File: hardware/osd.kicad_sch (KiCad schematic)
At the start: 12 parts, among them U14 SN74LVC1G3157, U15 TLV7031

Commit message: Trim BOM to strictly needed parts, fill sourcing fields, fix library datasheets
Owner review 2026-10-11, schematic only (board not resynced).

Removed (17 parts): D1 TVS (clamps above every IC abs max), R2/R3/C5
INA186 input RC, U5 TPS22810 O4 switch with C16/C129/R9/R10/R87/D2
(VHD pad now on +5V_BST, as Matrix HD boards; HD_EN still holds the
analog VTX off via Q28, R11 kept), R67 selector (PA_VCC is +BATT),
TH1/R70 PA NTC and R84 (patched-ELRS only; GPIO37/GPIO4 no-connect),
C92 and C121 (beyond SX1281 / LP5912 datasheet decoupling).

Changed: D4 WS2812 VDD to +5V (3.5 V min); X3 TCXO pin 1 floating per
the YXC sheet; C122/C123/C134 4.7 uF 0402 -> 0201 GRM035R60J475ME15D.

Sourcing: LCSC numbers for 21 MPN lines (SKUBAAE010 has no listing);
every BOM part keeps MPN + Manufacturer for NextPCB.

Library: 16 unused lib symbols pruned; dead or HTML-only datasheet
links replaced with verified PDF URLs (RTC6705, SE5004L, FL2, X1,
EFM8BB51, BC857BM, FTC252012, HCS1206 shunt, Molex 53047).

Net-class patterns and contract entries for the removed nets dropped;
PINMAP ESP32 rows updated (GPIO36 is ADC1_CH0).

Validation: ERC 0 errors / 2 warnings (baseline); check_netlist 7 ok;
sch_integrate --check idempotent; check_conventions unchanged.

Co-Authored-By: Claude Opus 5.5 <noreply@anthropic.com>
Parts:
- C66: LCSC (none) -> C76922
- R52: LCSC (none) -> C155736
- R54: LCSC (none) -> C295793
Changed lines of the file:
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@@
 		(in_pos_files no)
 		(dnp no)
-		(property "Reference" "#PWR147"
+		(property "Reference" "#PWR138"
 			(at 158.75 69.85 0)
 			(hide yes)
@@
 			(project "OpenAIO-Whoop"
 				(path "/2c3a7206-1e66-4d43-a02f-491225e20dd6/d622c956-8c4e-5ac1-b8c4-8a8024f124d6"
-					(reference "#PWR147")
+					(reference "#PWR138")
 					(unit 1)
 				)
@@
 		(in_pos_files no)
 		(dnp no)
-		(property "Reference" "#PWR148"
+		(property "Reference" "#PWR139"
 			(at 54.61 72.39 0)
 			(hide yes)
@@
 			(project "OpenAIO-Whoop"
 				(path "/2c3a7206-1e66-4d43-a02f-491225e20dd6/d622c956-8c4e-5ac1-b8c4-8a8024f124d6"
-					(reference "#PWR148")
+					(reference "#PWR139")
 					(unit 1)
 				)
@@
 		(in_pos_files no)
 		(dnp no)
-		(property "Reference" "#PWR157"
+		(property "Reference" "#PWR148"
 			(at 106.68 119.38 0)
 			(hide yes)
@@
 			(project "OpenAIO-Whoop"
 				(path "/2c3a7206-1e66-4d43-a02f-491225e20dd6/d622c956-8c4e-5ac1-b8c4-8a8024f124d6"
-					(reference "#PWR157")
+					(reference "#PWR148")
 					(unit 1)
 				)
@@
 		(in_pos_files no)
 		(dnp no)
-		(property "Reference" "#PWR149"
+		(property "Reference" "#PWR140"
 			(at 63.5 72.39 0)
 			(hide yes)
@@
 			(project "OpenAIO-Whoop"
 				(path "/2c3a7206-1e66-4d43-a02f-491225e20dd6/d622c956-8c4e-5ac1-b8c4-8a8024f124d6"
-					(reference "#PWR149")
+					(reference "#PWR140")
 					(unit 1)
 				)
@@
 		(in_pos_files no)
 		(dnp no)
-		(property "Reference" "#PWR158"
+		(property "Reference" "#PWR149"
 			(at 66.04 135.89 0)
 			(hide yes)
@@
 			(project "OpenAIO-Whoop"
 				(path "/2c3a7206-1e66-4d43-a02f-491225e20dd6/d622c956-8c4e-5ac1-b8c4-8a8024f124d6"
-					(reference "#PWR158")
+					(reference "#PWR149")
 					(unit 1)
 				)
@@
 		(in_pos_files no)
 		(dnp no)
-		(property "Reference" "#PWR146"
+		(property "Reference" "#PWR137"
 			(at 184.15 59.69 0)
 			(hide yes)
@@
 			(project "OpenAIO-Whoop"
 				(path "/2c3a7206-1e66-4d43-a02f-491225e20dd6/d622c956-8c4e-5ac1-b8c4-8a8024f124d6"
-					(reference "#PWR146")
+					(reference "#PWR137")
 					(unit 1)
 				)
@@
 			)
 		)
-		(property "LCSC" ""
+		(property "LCSC" "C155736"
 			(at 54.61 119.38 0)
 			(hide yes)
@@
 		(in_pos_files no)
 		(dnp no)
-		(property "Reference" "#PWR154"
+		(property "Reference" "#PWR145"
 			(at 106.68 93.98 0)
 			(hide yes)
@@
 			(project "OpenAIO-Whoop"
 				(path "/2c3a7206-1e66-4d43-a02f-491225e20dd6/d622c956-8c4e-5ac1-b8c4-8a8024f124d6"
-					(reference "#PWR154")
+					(reference "#PWR145")
 					(unit 1)
 				)
@@
 		(in_pos_files no)
 		(dnp no)
-		(property "Reference" "#PWR156"
+		(property "Reference" "#PWR147"
 			(at 66.04 113.03 0)
 			(hide yes)
@@
 			(project "OpenAIO-Whoop"
 				(path "/2c3a7206-1e66-4d43-a02f-491225e20dd6/d622c956-8c4e-5ac1-b8c4-8a8024f124d6"
-					(reference "#PWR156")
+					(reference "#PWR147")
 					(unit 1)
 				)
@@
 			)
 		)
-		(property "LCSC" ""
+		(property "LCSC" "C295793"
 			(at 66.04 125.73 0)
 			(hide yes)
@@
 			)
 		)
-		(property "LCSC" ""
+		(property "LCSC" "C76922"
 			(at 63.5 62.23 0)
 			(hide yes)
@@
 		(in_pos_files no)
 		(dnp no)
-		(property "Reference" "#PWR151"
+		(property "Reference" "#PWR142"
 			(at 125.73 72.39 0)
 			(hide yes)
@@
 			(project "OpenAIO-Whoop"
 				(path "/2c3a7206-1e66-4d43-a02f-491225e20dd6/d622c956-8c4e-5ac1-b8c4-8a8024f124d6"
-					(reference "#PWR151")
+					(reference "#PWR142")
 					(unit 1)
 				)
@@
 		(in_pos_files no)
 		(dnp no)
-		(property "Reference" "#PWR155"
+		(property "Reference" "#PWR146"
 			(at 91.44 100.33 0)
 			(hide yes)
@@
 			(project "OpenAIO-Whoop"
 				(path "/2c3a7206-1e66-4d43-a02f-491225e20dd6/d622c956-8c4e-5ac1-b8c4-8a8024f124d6"
-					(reference "#PWR155")
+					(reference "#PWR146")
 					(unit 1)
 				)
@@
 		(in_pos_files no)
 		(dnp no)
-		(property "Reference" "#PWR153"
+		(property "Reference" "#PWR144"
 			(at 91.44 90.17 0)
 			(hide yes)
@@
 			(project "OpenAIO-Whoop"
 				(path "/2c3a7206-1e66-4d43-a02f-491225e20dd6/d622c956-8c4e-5ac1-b8c4-8a8024f124d6"
-					(reference "#PWR153")
+					(reference "#PWR144")
 					(unit 1)
 				)
@@
 		(in_pos_files no)
 		(dnp no)
-		(property "Reference" "#PWR150"
+		(property "Reference" "#PWR141"
 			(at 93.98 72.39 0)
 			(hide yes)
@@
 			(project "OpenAIO-Whoop"
 				(path "/2c3a7206-1e66-4d43-a02f-491225e20dd6/d622c956-8c4e-5ac1-b8c4-8a8024f124d6"
-					(reference "#PWR150")
+					(reference "#PWR141")
 					(unit 1)
 				)
@@
 		(in_pos_files no)
 		(dnp no)
-		(property "Reference" "#PWR152"
+		(property "Reference" "#PWR143"
 			(at 176.53 72.39 0)
 			(hide yes)
@@
 			(project "OpenAIO-Whoop"
 				(path "/2c3a7206-1e66-4d43-a02f-491225e20dd6/d622c956-8c4e-5ac1-b8c4-8a8024f124d6"
-					(reference "#PWR152")
-					(unit 1)
-				)
+					(reference "#PWR143")
+					(unit 1)
+				)

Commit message: Footprint audit vs datasheets, 0201 lands to Murata minimum, schematic notes shortened
Footprints: 45 checked against their datasheets by group, no pin or
land errors. C/R/L_0201_..._L pad height 0.28 -> 0.30 (Murata GRM03
reflow table c >= 0.30); other lands already at least density per D109
and left unchanged. Land spec texts cleaned (sources, shared parts).

Schematic notes: 157 -> 152 items, 19.5k -> 9.7k characters, all
current (diode-OR, removed parts, RTC6705 filters, TX0/RX0).

check_footprint 107/107 lib specs PASS; ERC 0 errors / 2 warnings;
check_netlist 7 ok; sch_integrate --check clean. Board not synced.

Co-Authored-By: Claude Opus 5.5 <noreply@anthropic.com>
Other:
- note added: "Comparator: OSD_SYNC low during sync (GPIO23, PIO2)"
- note added: "OSD_W selects white (high) or black (low) through the divider"
- note added: "Sync detection: sync tips clamped to -VF"
- note added: "U15 V+ (2) is decoupled by C70, shared with U14"
- note removed: "Comparator: OSD_SYNC low during sync, read by RP2354A PIO2 (GPIO23)"
- note removed: "Resistor divider lets the OSD_W GPIO select white (high: 1.05 V) or black (low: 0.27 V)"
- note removed: "Sync detection, VID_DC sync tips clamped to -VF (about -0.1..-0.2 V)"
- note removed: "U15 V+ (2) is decoupled by C70 in the switch cell, one 100n shared with U14 (BR-13)"
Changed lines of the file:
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@@
 		)
 	)
-	(text "Resistor divider lets the OSD_W GPIO select\nwhite (high: 1.05 V) or black (low: 0.27 V)"
+	(text "OSD_W selects white (high) or black (low) through the divider"
 		(exclude_from_sim no)
 		(at 44.958 88.392 0)
@@
 		)
 	)
-	(text "U15 V+ (2) is decoupled by C70 in the switch cell,\none 100n shared with U14 (BR-13)"
+	(text "U15 V+ (2) is decoupled by C70, shared with U14"
 		(exclude_from_sim no)
 		(at 163.83 35.56 0)
@@
 		)
 	)
-	(text "Sync detection, VID_DC sync tips\nclamped to -VF (about -0.1..-0.2 V)"
+	(text "Sync detection: sync tips clamped to -VF"
 		(exclude_from_sim no)
 		(at 157.988 20.828 0)
@@
 		)
 	)
-	(text "Comparator: OSD_SYNC low during sync,\nread by RP2354A PIO2 (GPIO23)"
+	(text "Comparator: OSD_SYNC low during sync (GPIO23, PIO2)"
 		(exclude_from_sim no)
 		(at 164.338 74.676 0)
@@
 		)
 	)
-	(text_box "Placement: C70 is the one supply cap of U14 and U15, place it between them. Video entry parts R51/C66 at the CAM pad line; video on L1/L6 over GND, never L3; away from the boost (D69). Analog class on the video nets; OSD_W / OSD_EN Default."
+	(text_box "C70 is the one supply cap of U14 and U15: place it between them. R51/C66 at the CAM pad line; video on L1/L6 over GND, away from the boost."
 		(exclude_from_sim no)
 		(at 15.24 149.86 0)
@@
 		)
 	)
-	(text_box "Copied from OpenFC-Lite-Mini osd (flown): 75R termination, 680R/470p chroma filter, sync-tip clamp, TLV7031 sync comparator, SN74LVC1G3157 camera/OSD switch. Changed: COS8051 buffer deleted, divider R52-R54 about 5x lower (P4-10), one shared C70 (D52).\nOperation: OSD_EN low (reset) -> camera passes through; OSD_EN high -> OSD_W high = white, low = black. No OSD without camera sync. OSD_W/EN/SYNC = GPIO21/22/23 (PIO2).\nC68 X5R carries <= 0.6 V DC, no DC-bias loss (D69)."
+	(text_box "OSD_EN low (reset): camera passes through. OSD_EN high: OSD_W high = white, low = black. No OSD without camera sync.\nOSD_W/EN/SYNC = GPIO21/22/23 (PIO2)."
 		(exclude_from_sim no)
 		(at 200.66 17.78 0)
@@
 		)
 	)
-	(text_box "VIDEO_OUT drives the VTX video network directly (house buffer deleted). Loaded OSD levels: black about 0.24 V, white about 0.92 V; OSD text slightly softer than the camera, accepted. V9 checks on a monitor; fallback: rescale R52-R54 within the 3 mA OSD_W budget."
+	(text_box "VIDEO_OUT drives the VTX video network directly. Loaded levels: black about 0.24 V, white about 0.92 V."
 		(exclude_from_sim no)
 		(at 133.35 86.36 0)

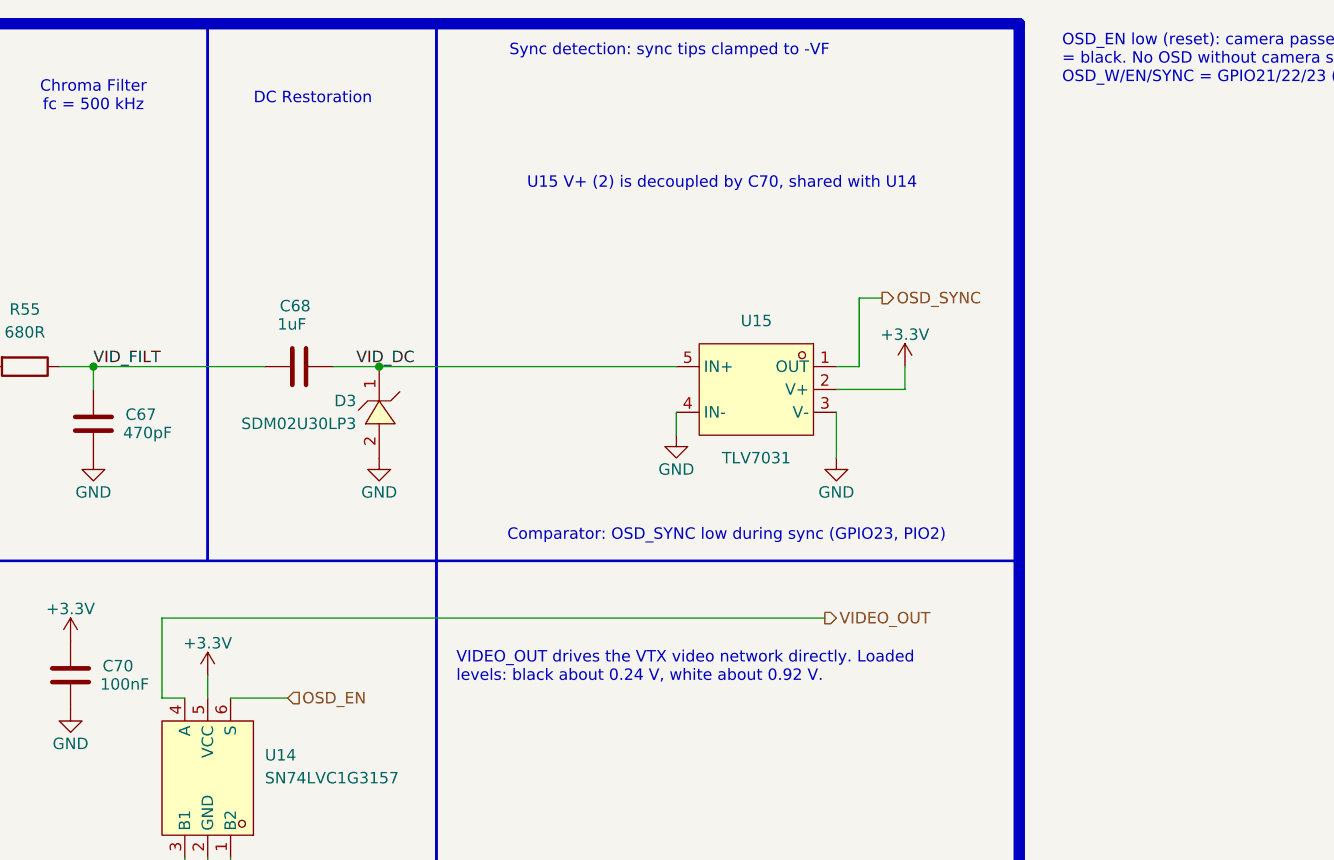
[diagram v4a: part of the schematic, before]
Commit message: WIP placement and schematic snapshot for shared routing
Owner placement and schematic edits, firmware bindings, routing notes and
board tooling, so others can try the routing. Not DRC-clean; PCB not yet
updated from the schematic (R1 to R2, C1/C2/C134 removal).

Co-Authored-By: Claude Opus 5.5 <noreply@anthropic.com>
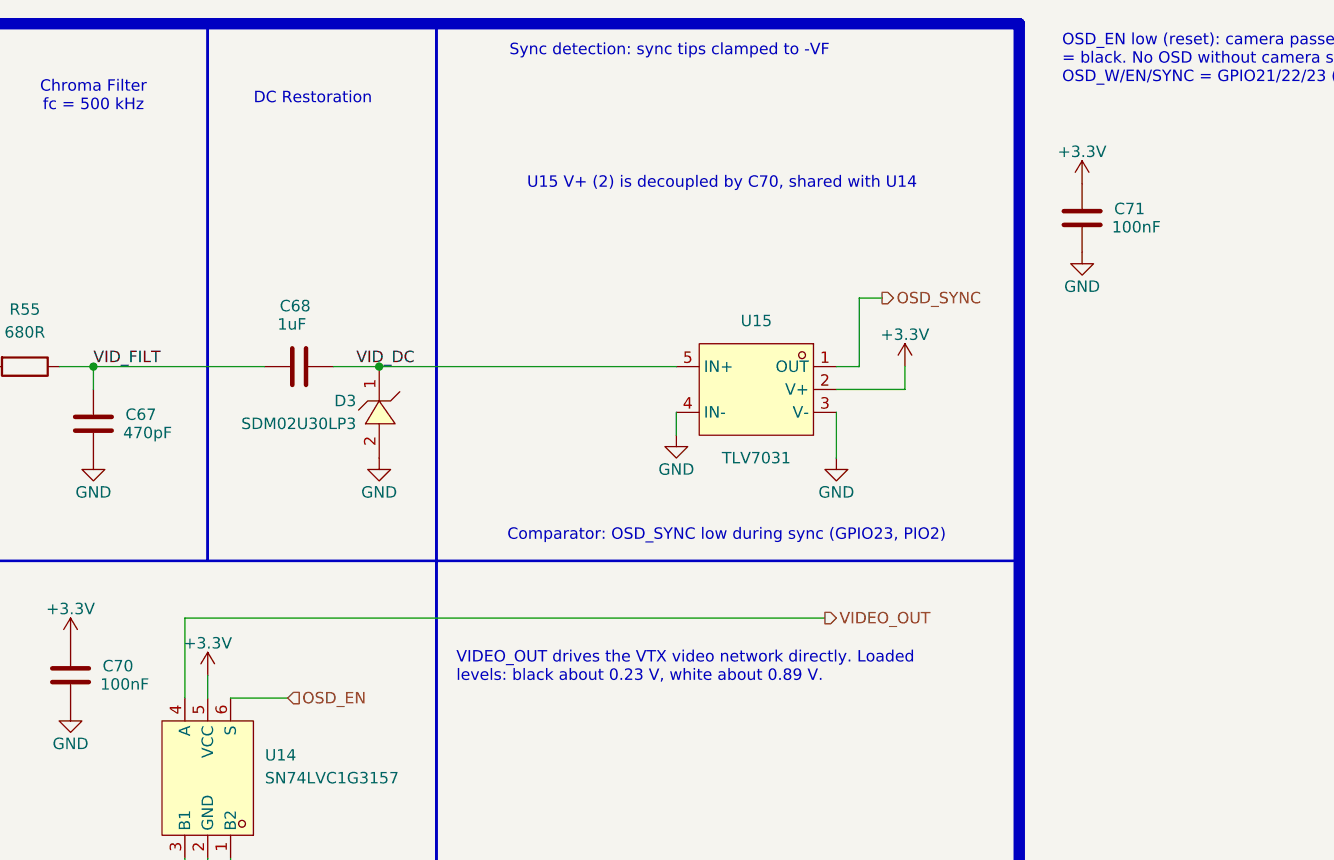
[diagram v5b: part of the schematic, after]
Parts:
- added C71: 100nF, lib:C_0201_0603Metric_L, symbol Device:C
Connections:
- net +3.3V: now also C71.1
- net GND: now also C71.2

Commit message: Every schematic symbol project-local (Device, power, Connector, Mechanical moved into lib)
tools/localise_symbols.py from OpenAIO. Netlist identical, ERC unchanged (0 errors, 24 warnings), every symbol, footprint and 3D model resolves inside the repo.

Co-Authored-By: Claude Opus 5.5 <noreply@anthropic.com>
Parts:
- C66, C67, C68, C70, C71: symbol Device:C -> lib:C
- R51, R52, R53, R54, R55: symbol Device:R -> lib:R
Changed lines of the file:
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@@
 	)
 	(symbol
-		(lib_id "power:GND")
+		(lib_id "lib:GND")
 		(at 158.75 63.5 0)
 		(unit 1)
@@
 	)
 	(symbol
-		(lib_id "power:GND")
+		(lib_id "lib:GND")
 		(at 54.61 66.04 0)
 		(unit 1)
@@
 	)
 	(symbol
-		(lib_id "Device:C")
+		(lib_id "lib:C")
 		(at 203.835 39.37 0)
 		(unit 1)
@@
 	)
 	(symbol
-		(lib_id "power:GND")
+		(lib_id "lib:GND")
 		(at 106.68 113.03 0)
 		(unit 1)
@@
 	)
 	(symbol
-		(lib_id "power:GND")
+		(lib_id "lib:GND")
 		(at 63.5 66.04 0)
 		(unit 1)
@@
 	)
 	(symbol
-		(lib_id "Device:R")
+		(lib_id "lib:R")
 		(at 54.61 62.23 0)
 		(unit 1)
@@
 	)
 	(symbol
-		(lib_id "power:GND")
+		(lib_id "lib:GND")
 		(at 66.04 129.54 0)
 		(unit 1)
@@
 	)
 	(symbol
-		(lib_id "power:+3.3V")
+		(lib_id "lib:+3.3V")
 		(at 203.835 35.56 0)
 		(unit 1)
@@
 	)
 	(symbol
-		(lib_id "power:+3.3V")
+		(lib_id "lib:+3.3V")
 		(at 184.15 55.88 0)
 		(unit 1)
@@
 	)
 	(symbol
-		(lib_id "Device:C")
+		(lib_id "lib:C")
 		(at 116.84 55.88 90)
 		(unit 1)
@@
 	)
 	(symbol
-		(lib_id "Device:R")
+		(lib_id "lib:R")
 		(at 54.61 119.38 90)
 		(unit 1)
@@
 	)
 	(symbol
-		(lib_id "Device:C")
+		(lib_id "lib:C")
 		(at 91.44 90.17 0)
 		(unit 1)
@@
 	)
 	(symbol
-		(lib_id "power:+3.3V")
+		(lib_id "lib:+3.3V")
 		(at 106.68 90.17 0)
 		(unit 1)
@@
 	)
 	(symbol
-		(lib_id "power:+3.3V")
+		(lib_id "lib:+3.3V")
 		(at 66.04 109.22 0)
 		(unit 1)
@@
 	)
 	(symbol
-		(lib_id "power:GND")
+		(lib_id "lib:GND")
 		(at 203.835 43.18 0)
 		(unit 1)
@@
 	)
 	(symbol
-		(lib_id "Device:R")
+		(lib_id "lib:R")
 		(at 66.04 113.03 180)
 		(unit 1)
@@
 	)
 	(symbol
-		(lib_id "Device:R")
+		(lib_id "lib:R")
 		(at 66.04 125.73 180)
 		(unit 1)
@@
 	)
 	(symbol
-		(lib_id "Device:C")
+		(lib_id "lib:C")
 		(at 93.98 62.23 0)
 		(unit 1)
@@
 	)
 	(symbol
-		(lib_id "Device:C")
+		(lib_id "lib:C")
 		(at 63.5 62.23 0)
 		(unit 1)
@@
 	)
 	(symbol
-		(lib_id "power:GND")
+		(lib_id "lib:GND")
 		(at 125.73 66.04 0)
 		(unit 1)
@@
 	)
 	(symbol
-		(lib_id "power:GND")
+		(lib_id "lib:GND")
 		(at 91.44 93.98 0)
 		(unit 1)
@@
 	)
 	(symbol
-		(lib_id "power:+3.3V")
+		(lib_id "lib:+3.3V")
 		(at 91.44 86.36 0)
 		(unit 1)
@@
 	)
 	(symbol
-		(lib_id "Device:R")
+		(lib_id "lib:R")
 		(at 86.36 55.88 270)
 		(unit 1)
@@
 	)
 	(symbol
-		(lib_id "power:GND")
+		(lib_id "lib:GND")
 		(at 93.98 66.04 0)
 		(unit 1)
@@
 	)
 	(symbol
-		(lib_id "power:GND")
+		(lib_id "lib:GND")
 		(at 176.53 66.04 0)
 		(unit 1)
